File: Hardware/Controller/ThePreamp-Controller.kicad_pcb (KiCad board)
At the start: 2 copper layers, 302.5 x 44.5 mm, 27 parts, among them J1 8V, J2 Power relay trigger, J3 SPI DISPLAY 1, J4 SPI DISPLAY 2, J5 Digital Out, J6 3.3V (Opt), J7 Conn_01x03_Pin, SW1 RotaryEncoder_Switch, SW2 RotaryEncoder_Switch, U1 TSOP34838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

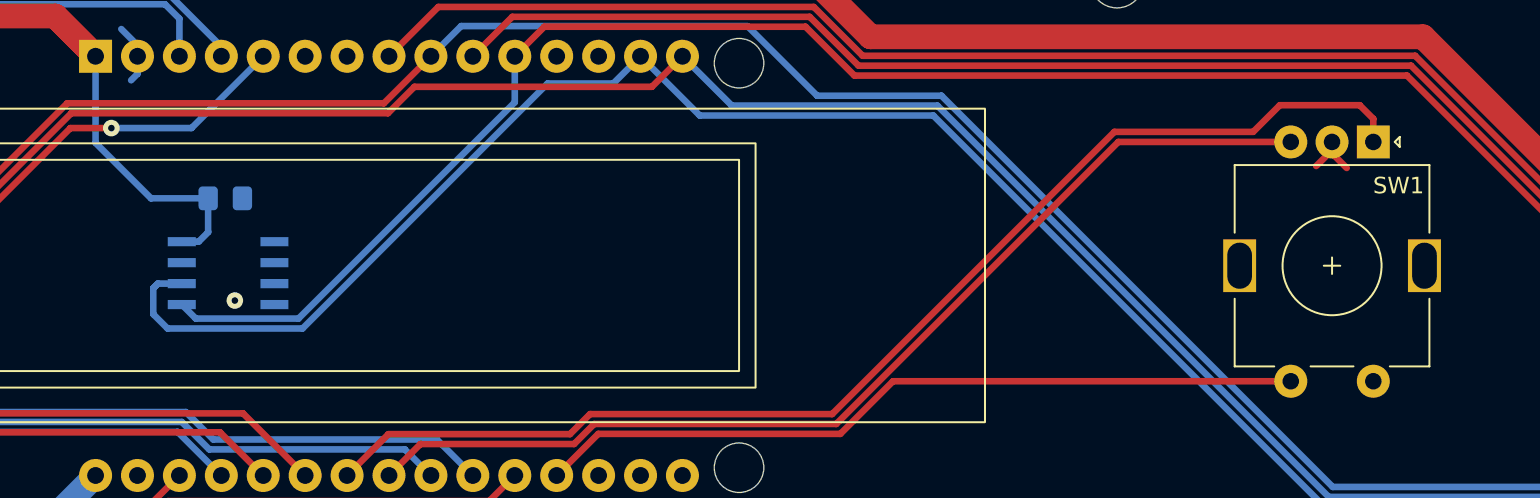
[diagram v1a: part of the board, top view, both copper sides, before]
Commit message: Updated Template-Daughter-board to reflect changes
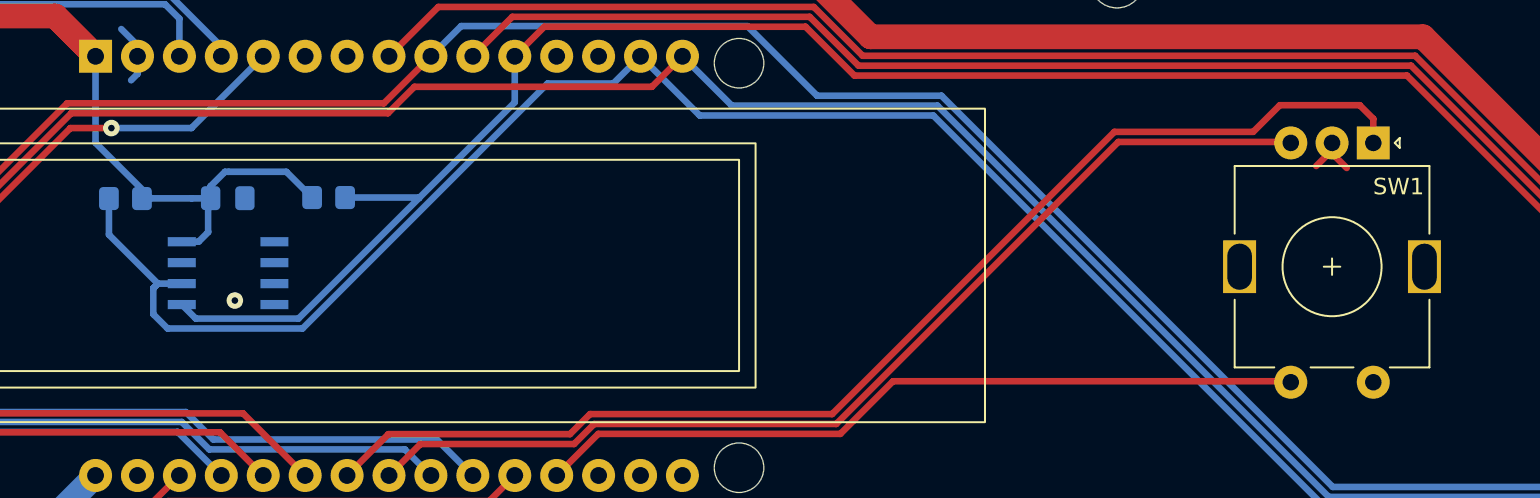
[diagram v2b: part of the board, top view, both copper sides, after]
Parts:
- added R2: 2K2, Resistor_SMD:R_0805_2012Metric_Pad1.20x1.40mm_HandSolder, B.Cu at (195.3, 60.5)
- added R3: 2K2, Resistor_SMD:R_0805_2012Metric_Pad1.20x1.40mm_HandSolder, B.Cu at (207.6, 60.4)
- moved C1 0.15 mm to (201.5, 60.5)
- moved SW1 0.06 mm to (270.9, 57.1)
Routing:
- net +3V3 ESP32: track 35.8 -> 43.7 mm
- net I2C:SCL: track 140.5 -> 146.8 mm
- net I2C:SDA: track 133.5 -> 137.9 mm

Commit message: Connector placement in chassis
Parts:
- moved J1 215.3 mm to (282.4, 82.5)
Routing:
- net +8V: track 137.5 -> 112.1 mm
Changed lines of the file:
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@@
 	(footprint "THE_PREAMP_CONN_POWER_5_08:TBP01R2-508-02BK (VERT)"
 		(layer "B.Cu")
-		(at 67.08 82.5375 180)
+		(at 282.4 82.51 180)
 		(property "Reference" "J1"
 			(at -0.06 3.2775 0)
@@
 		)
 		(property "Value" "2K2"
-			(at 0 -1.65 360)
+			(at 0 -1.65 0)
 			(layer "B.Fab")
 			(effects
@@
 		)
 		(fp_text user "${REFERENCE}"
-			(at 0 0 360)
+			(at 0 0 0)
 			(layer "B.Fab")
 			(effects
@@
 	)
 	(segment
-		(start 183.39 84.93)
-		(end 177.3 84.93)
-		(width 1.5)
-		(layer "B.Cu")
-		(net 5)
-	)
-	(segment
 		(start 180.404698 84.93)
 		(end 179.357349 83.882651)
@@
 	)
 	(segment
-		(start 185.82 84.93)
-		(end 183.39 84.93)
+		(start 282.4 82.51)
+		(end 279.47 85.44)
 		(width 1.5)
 		(layer "B.Cu")
@@
 	)
 	(segment
-		(start 177.3 84.93)
-		(end 69.4725 84.93)
+		(start 185.82 84.93)
+		(end 193.5 77.25)
 		(width 1.5)
 		(layer "B.Cu")
@@
 	)
 	(segment
-		(start 193.5 77.25)
+		(start 180.404698 84.93)
 		(end 185.82 84.93)
 		(width 1.5)
@@
 	)
 	(segment
-		(start 177.3 84.93)
-		(end 178.31 84.93)
-		(width 1.5)
-		(layer "B.Cu")
-		(net 5)
-	)
-	(segment
-		(start 178.31 84.93)
-		(end 179.357349 83.882651)
+		(start 279.47 85.44)
+		(end 200.275787 85.44)
 		(width 1.5)
 		(layer "B.Cu")
@@
 	)
 	(segment
-		(start 69.4725 84.93)
-		(end 67.08 82.5375)
+		(start 200.275787 85.44)
+		(end 193.5 78.664213)
 		(width 1.5)
 		(layer "B.Cu")
@@
 	)
 	(segment
-		(start 183.39 84.93)
-		(end 180.404698 84.93)
+		(start 193.5 78.664213)
+		(end 193.5 77.25)
 		(width 1.5)
 		(layer "B.Cu")

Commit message: Pcb dimensions
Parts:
- added J8: 12V, THE_PREAMP_CONN_POWER_5_08:TBP01R2-508-02BK (VERT), B.Cu at (34.7, 82.5)
- moved J1 214.9 mm to (67.5, 82.5)
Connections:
- J5 pad 14: GND -> +12V
- J5 pad 16: GND -> +12V
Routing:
- net +8V: track 112.1 -> 129.4 mm
- net GND: track 28.5 -> 23.2 mm
- net +12V: track 0.00 -> 2.54 mm

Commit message: Chassis placement new draft
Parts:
- moved J5 33.7 mm to (325.9, 80.5)
- moved G*** 11.2 mm to (308.7, 55.6)
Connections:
- J5 pad 10: GND -> +3V3
- J5 pad 14: +12V -> GND
- J5 pad 16: +12V -> GND
- J5 pad 2: GND -> +12V
- J5 pad 4: GND -> +12V
- J5 pad 6: GND -> +12V
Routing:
- net SPI:MISO: track 99.9 -> 137.8 mm
- net SPI:SCK: track 257.1 -> 294.4 mm
- net +3V3: track 290.7 -> 327.0 mm
- net SPI:SS_MUSES: track 111.6 -> 146.3 mm
- net I2C:SDA: track 137.9 -> 171.7 mm
- net SPI:MOSI: track 252.4 -> 286.1 mm
- net I2C:SCL: track 146.8 -> 180.6 mm
- net GND: track 23.2 -> 14.5 mm
- net +12V: track 2.54 -> 0.00 mm
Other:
- board size 302.5 x 44.5 mm -> 335.9 x 44.5 mm
- board text added: "12V"

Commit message: Updated pcb 3.3V + adjust of connectors on controller pcb
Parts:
- removed J7: Conn_01x03_Pin, Connector_PinHeader_2.54mm:PinHeader_1x03_P2.54mm_Vertical
- moved J8 262.6 mm to (297.3, 82.1)
- moved J6 249.9 mm to (272.1, 82.1)
- moved J1 217.3 mm to (284.7, 82.1)
- moved J2 32.3 mm to (22.2, 82.5)
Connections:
- J6 pad 1: Net-(J7-Pin_3) -> +3.3V
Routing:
- net Net-(J7-Pin_3): track 186.7 -> 0.00 mm
- net +8V: track 129.4 -> 17.3 mm
- net +3V3 ESP32: track 43.7 -> 25.2 mm
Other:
- board text added: "+12V"
- board text added: "+3.3V"
- board text removed: "+3V3 Power"
- board text removed: "External"
- board text removed: "Internal"

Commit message: Ready for review (updated Digital PSU - Transformer and Controller)
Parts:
- U4: footprint APC_817B1_SL:APC-817xx-SL_AMB-M -> Package_DIP:DIP-4_W7.62mm
- moved C6 63.6 mm to (243.0, 82.8)
- moved U4 33.9 mm to (16.3, 67.5)
- moved R1 32.8 mm to (17.6, 62.4)
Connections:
- J6 pad 1: +3.3V -> +3V3
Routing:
- net +8V: track 17.3 -> 97.5 mm
- net +3V3: track 327.0 -> 383.9 mm
- net Net-(U3-D2): track 156.9 -> 191.1 mm
- net +12V: track 0.00 -> 34.0 mm
- net SPI:MISO: track 137.8 -> 130.8 mm
- net I2C:SCL: track 180.6 -> 174.5 mm
- net Net-(J2-Pad2): track 12.9 -> 7.64 mm
- net GND: track 14.5 -> 19.2 mm
- net Net-(J2-Pad1): track 12.5 -> 8.70 mm
- net SPI:SCK: track 294.4 -> 290.9 mm
- net Net-(R1-Pad1): track 3.19 -> 5.17 mm
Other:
- board text added: "2024-04"
- board text removed: "+3.3V"
- board text removed: "2024-03"
